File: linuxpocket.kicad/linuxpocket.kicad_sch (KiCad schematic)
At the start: 0 parts

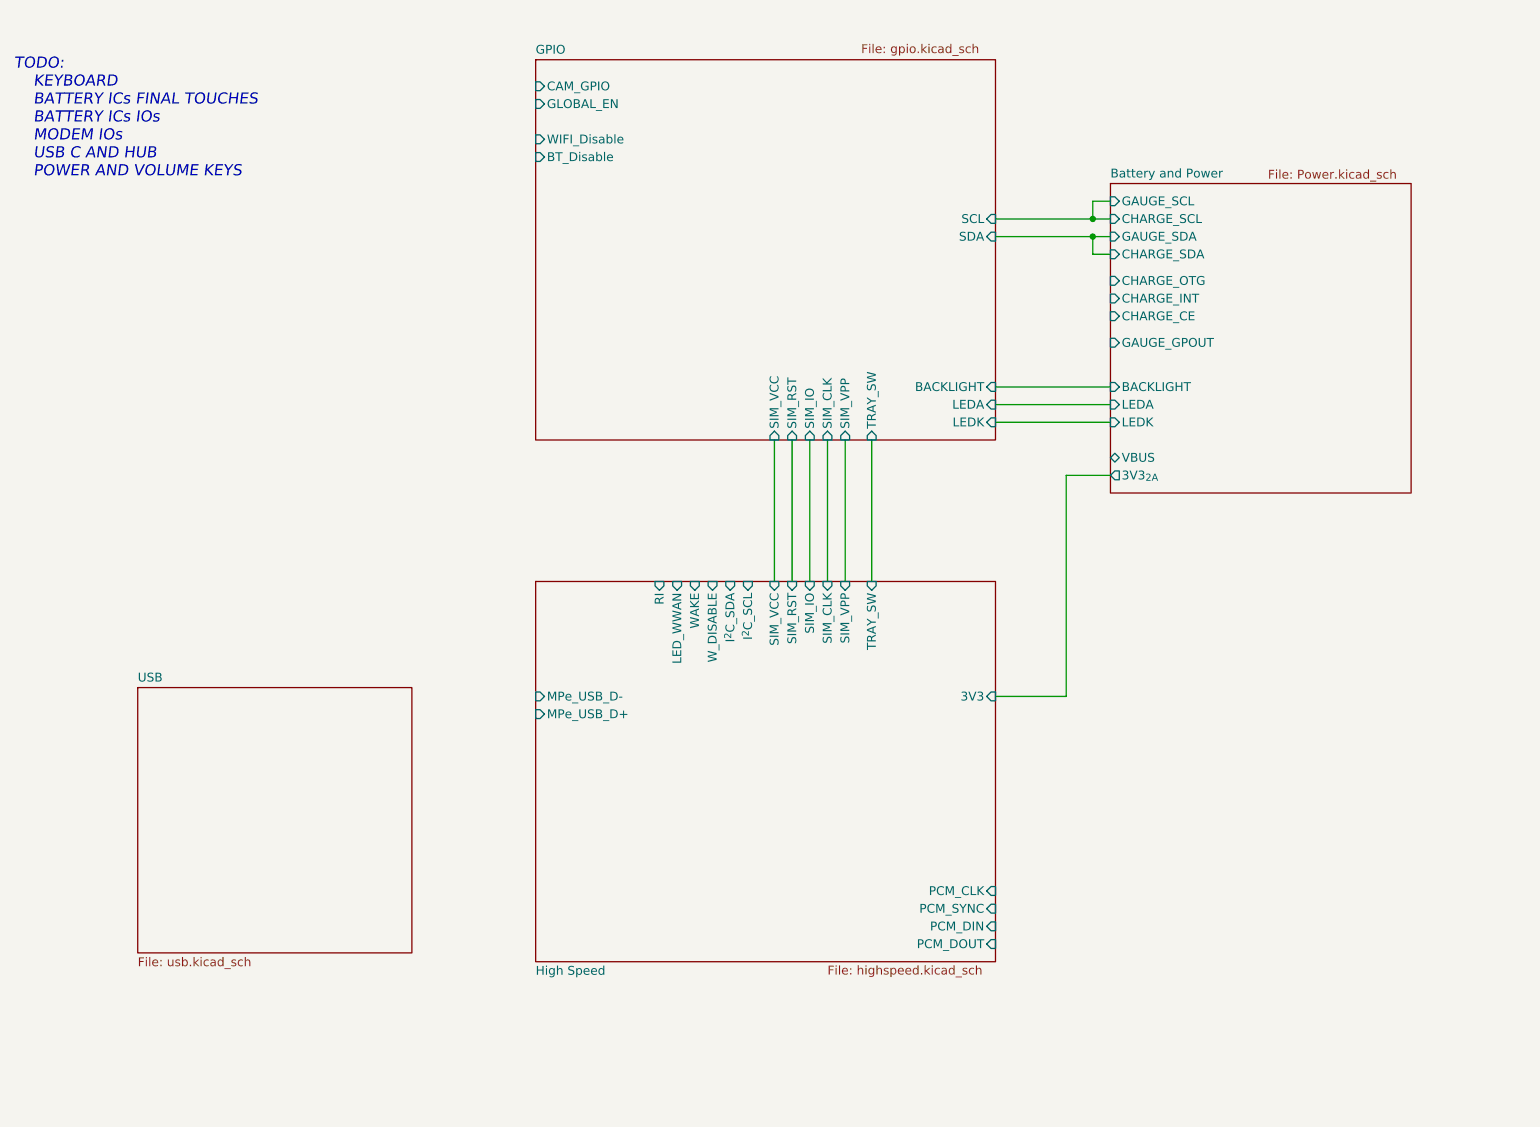
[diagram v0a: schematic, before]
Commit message: Add keyboard, improve many things etc.
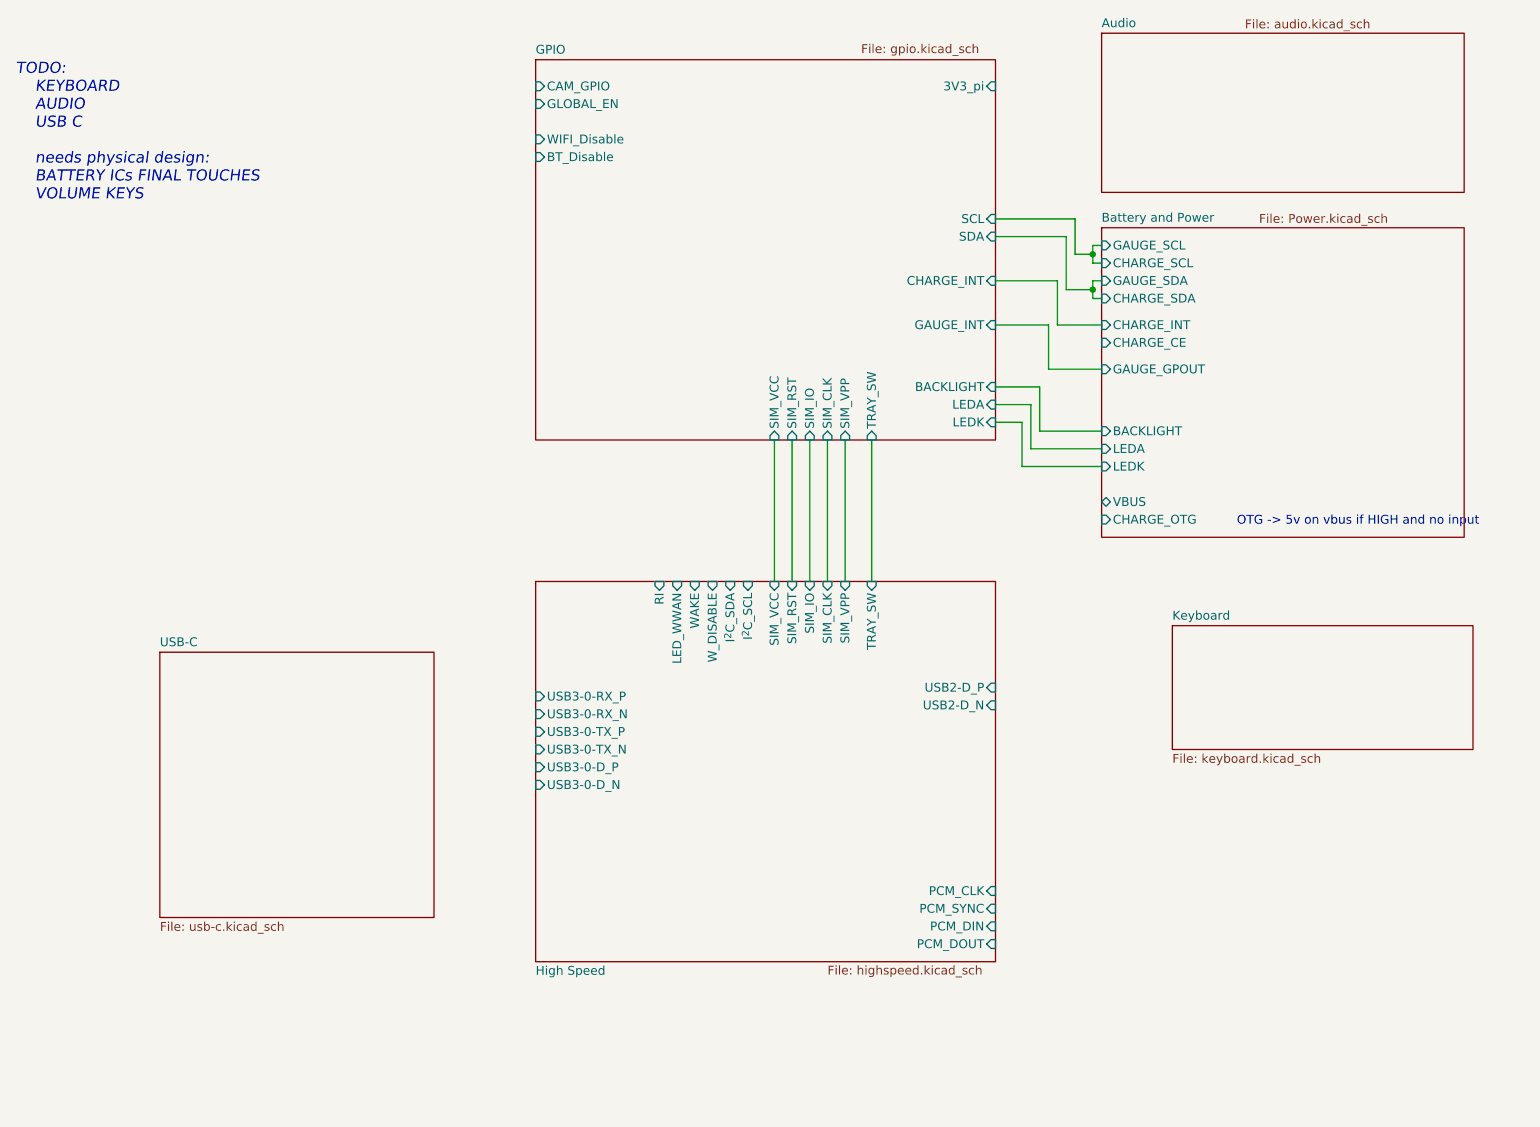
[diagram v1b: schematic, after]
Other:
- sheet USB renamed USB-C
- added sheet Audio (audio.kicad_sch)
- added sheet Keyboard (keyboard.kicad_sch)
- sheet Battery and Power ports: added none; removed 3V3_{2A}
- sheet GPIO ports: added 3V3_pi, CHARGE_INT, GAUGE_INT; removed none
- sheet High Speed ports: added USB2-D_N, USB2-D_P, USB3-0-D_N, USB3-0-D_P, USB3-0-RX_N, USB3-0-RX_P, USB3-0-TX_N, USB3-0-TX_P; removed 3V3, MPe_USB_D+, MPe_USB_D-
- sheet USB-C: file usb.kicad_sch -> usb-c.kicad_sch
- note added: "OTG -> 5v on vbus if HIGH and no input"
- note added: "TODO: KEYBOARD AUDIO USB C needs physical design: BATTERY ICs FINAL TOUCHES VOLUME KEYS"
- note removed: "TODO: KEYBOARD BATTERY ICs FINAL TOUCHES BATTERY ICs IOs MODEM IOs USB C AND HUB POWER AND VOLUME KEYS"

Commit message: Start with HDMI connector.
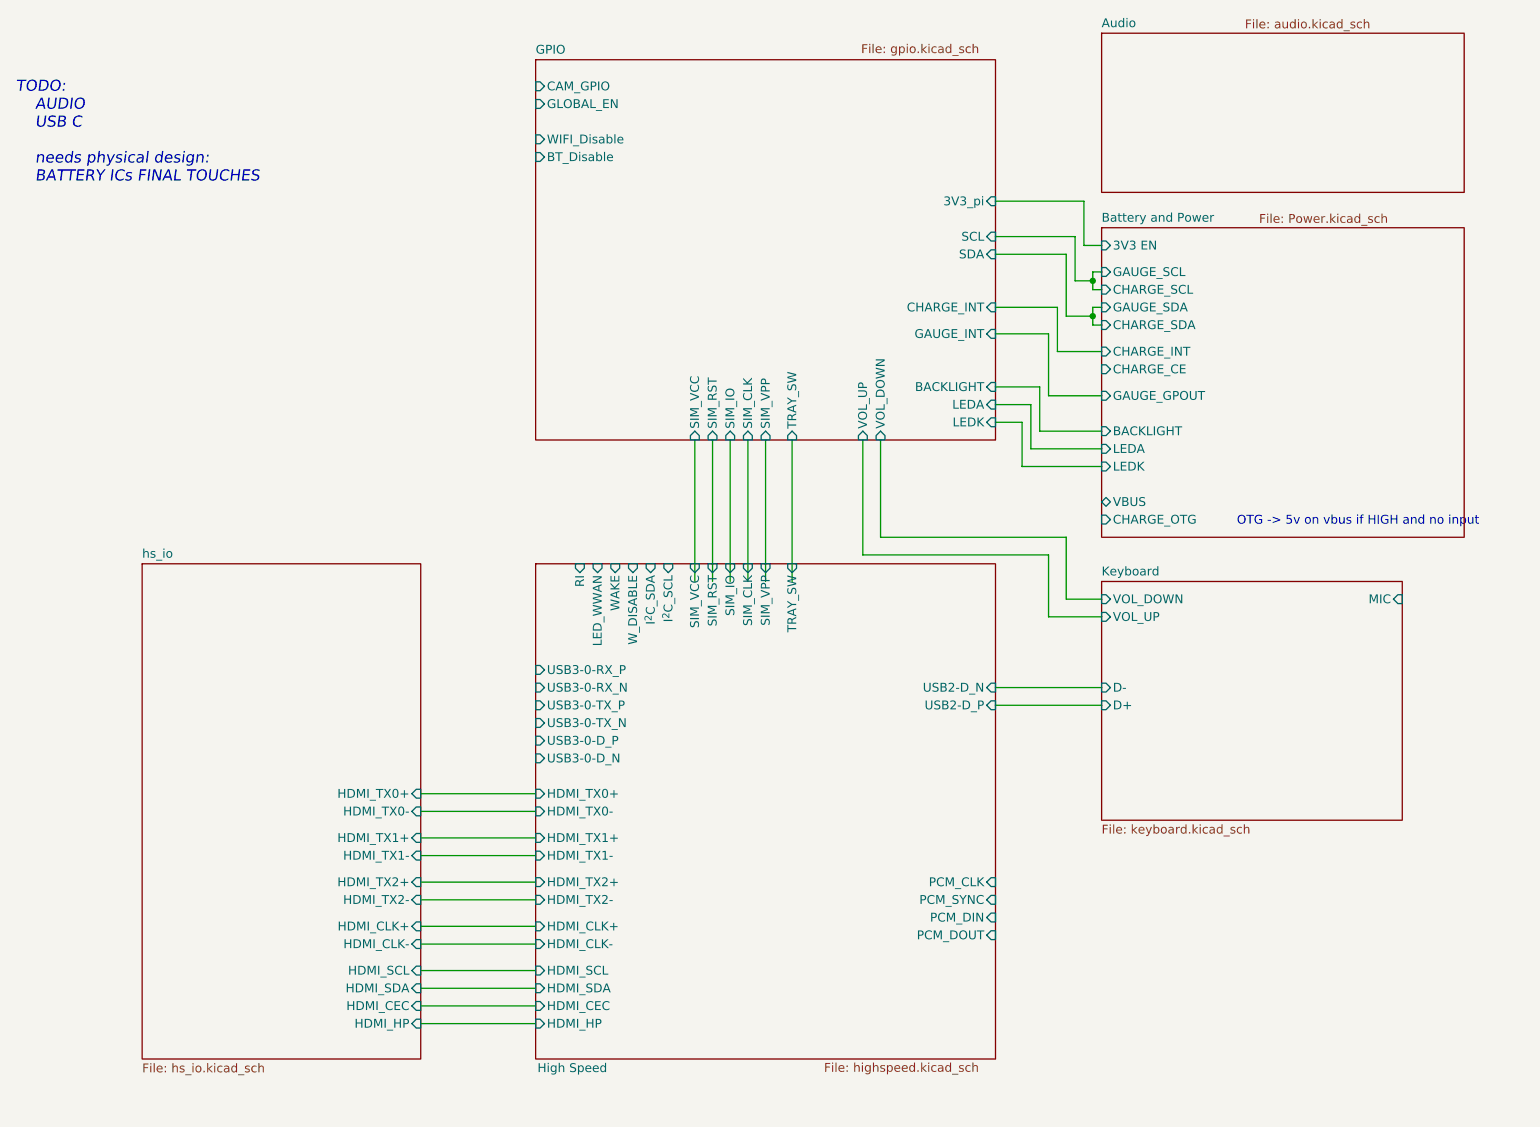
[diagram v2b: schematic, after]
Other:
- sheet USB-C renamed hs_io
- sheet Battery and Power ports: added 3V3 EN; removed none
- sheet GPIO ports: added VOL_DOWN, VOL_UP; removed none
- sheet High Speed ports: added HDMI_CEC, HDMI_CLK+, HDMI_CLK-, HDMI_HP, HDMI_SCL, HDMI_SDA, HDMI_TX0+, HDMI_TX0-, HDMI_TX1+, HDMI_TX1-, HDMI_TX2+, HDMI_TX2-; removed none
- sheet Keyboard ports: added D+, D-, MIC, VOL_DOWN, VOL_UP; removed none
- sheet hs_io: file usb-c.kicad_sch -> hs_io.kicad_sch
- sheet hs_io ports: added HDMI_CEC, HDMI_CLK+, HDMI_CLK-, HDMI_HP, HDMI_SCL, HDMI_SDA, HDMI_TX0+, HDMI_TX0-, HDMI_TX1+, HDMI_TX1-, HDMI_TX2+, HDMI_TX2-; removed none
- note added: "TODO: AUDIO USB C needs physical design: BATTERY ICs FINAL TOUCHES"
- note removed: "TODO: KEYBOARD AUDIO USB C needs physical design: BATTERY ICs FINAL TOUCHES VOLUME KEYS"

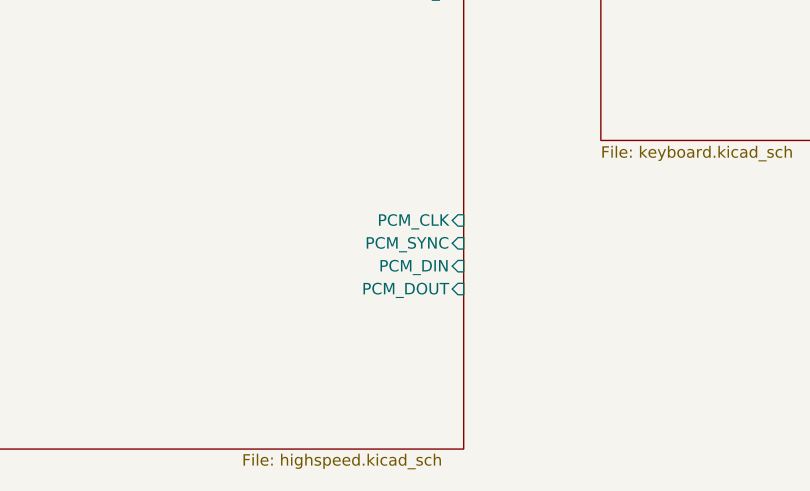
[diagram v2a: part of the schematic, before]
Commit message: Finish HDMI
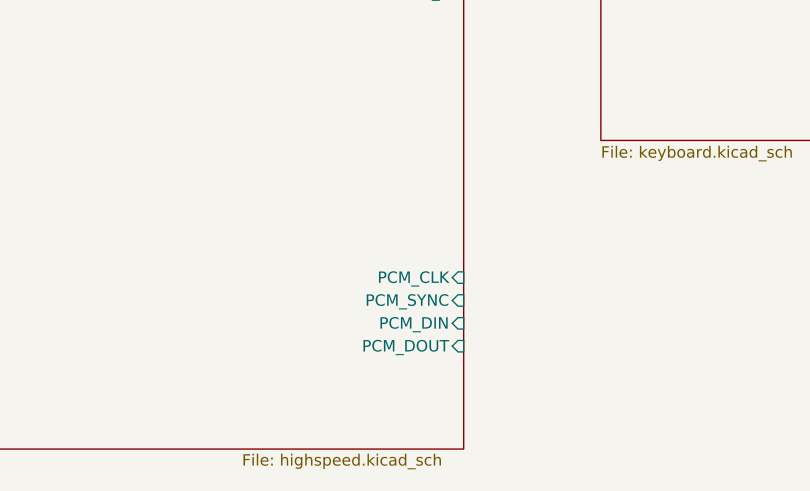
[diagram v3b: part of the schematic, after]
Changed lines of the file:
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@@
 	(title_block
 		(title "Overview")
-		(date "2024-19-10 - 2024-31-10")
+		(date "2024-10-19 - 2025-01-29")
 		(rev "Prototype v0")
 		(company "xamuel.xyz")
@@
 		)
 		(pin "PCM_DOUT" input
-			(at 172.72 154.94 0)
+			(at 172.72 161.29 0)
 			(effects
 				(font
@@
 		)
 		(pin "PCM_DIN" input
-			(at 172.72 152.4 0)
+			(at 172.72 158.75 0)
 			(effects
 				(font
@@
 		)
 		(pin "PCM_SYNC" input
-			(at 172.72 149.86 0)
+			(at 172.72 156.21 0)
 			(effects
 				(font
@@
 		)
 		(pin "PCM_CLK" input
-			(at 172.72 147.32 0)
-			(effects
-				(font
+			(at 172.72 153.67 0)
+			(effects
+				(font

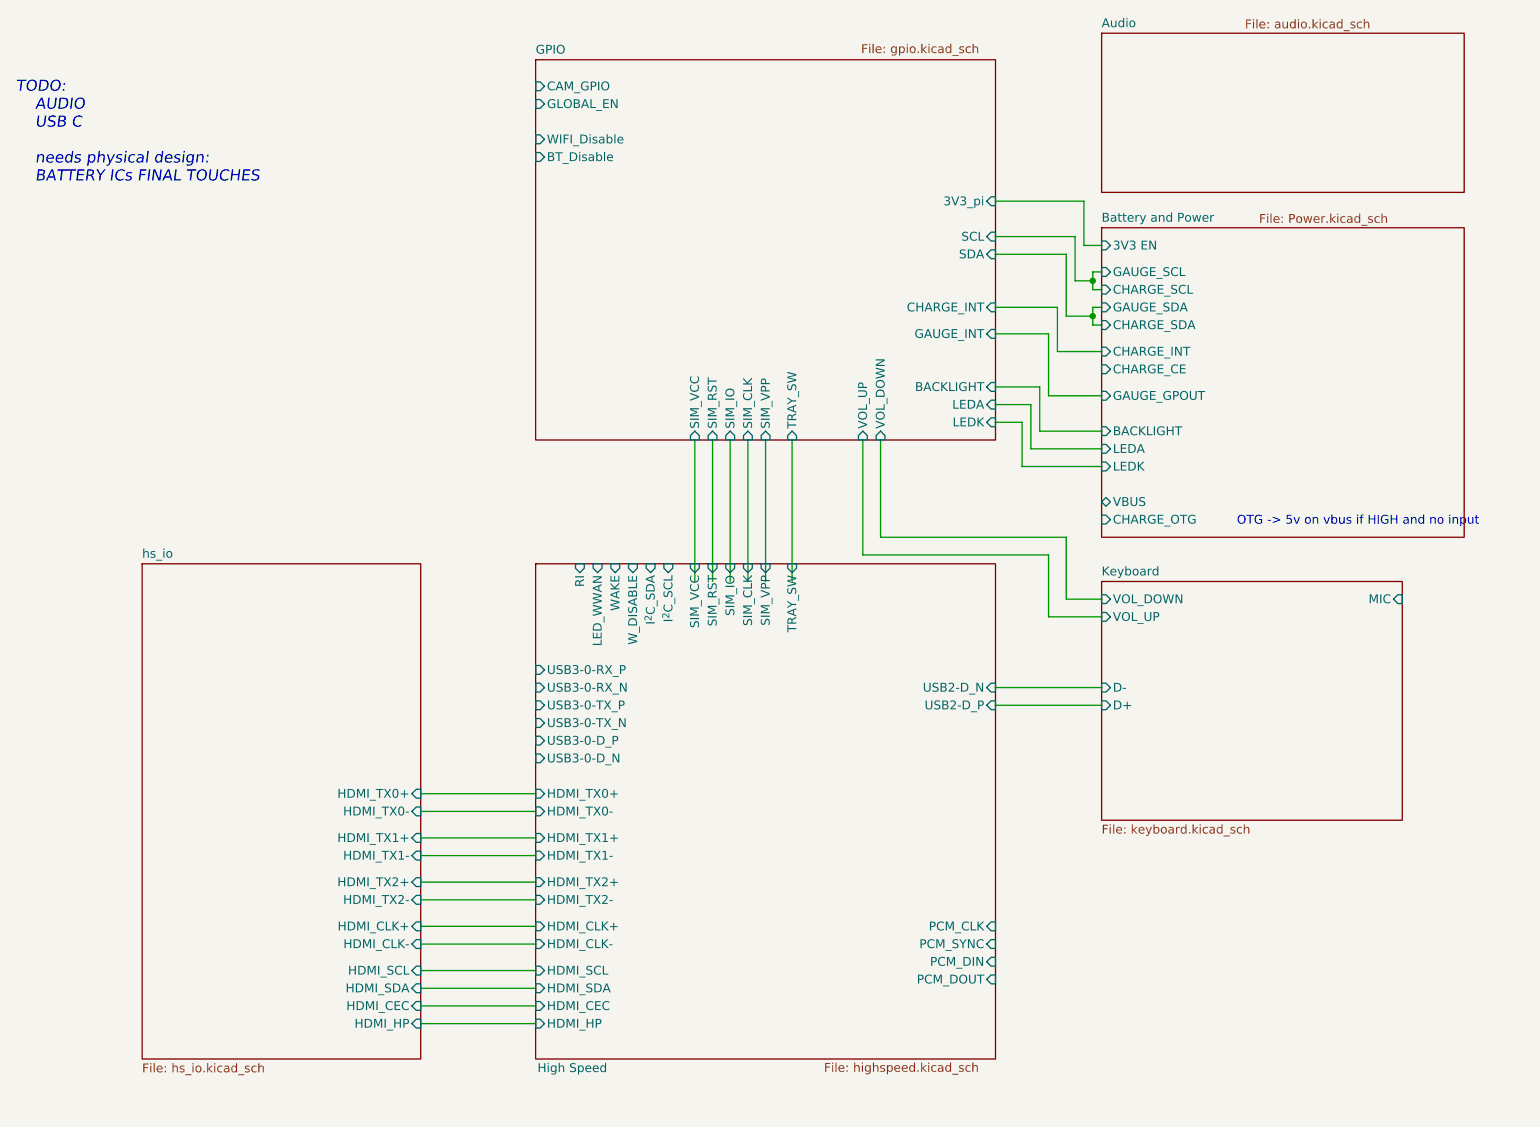
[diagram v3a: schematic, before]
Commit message: Finish USB-C. #1
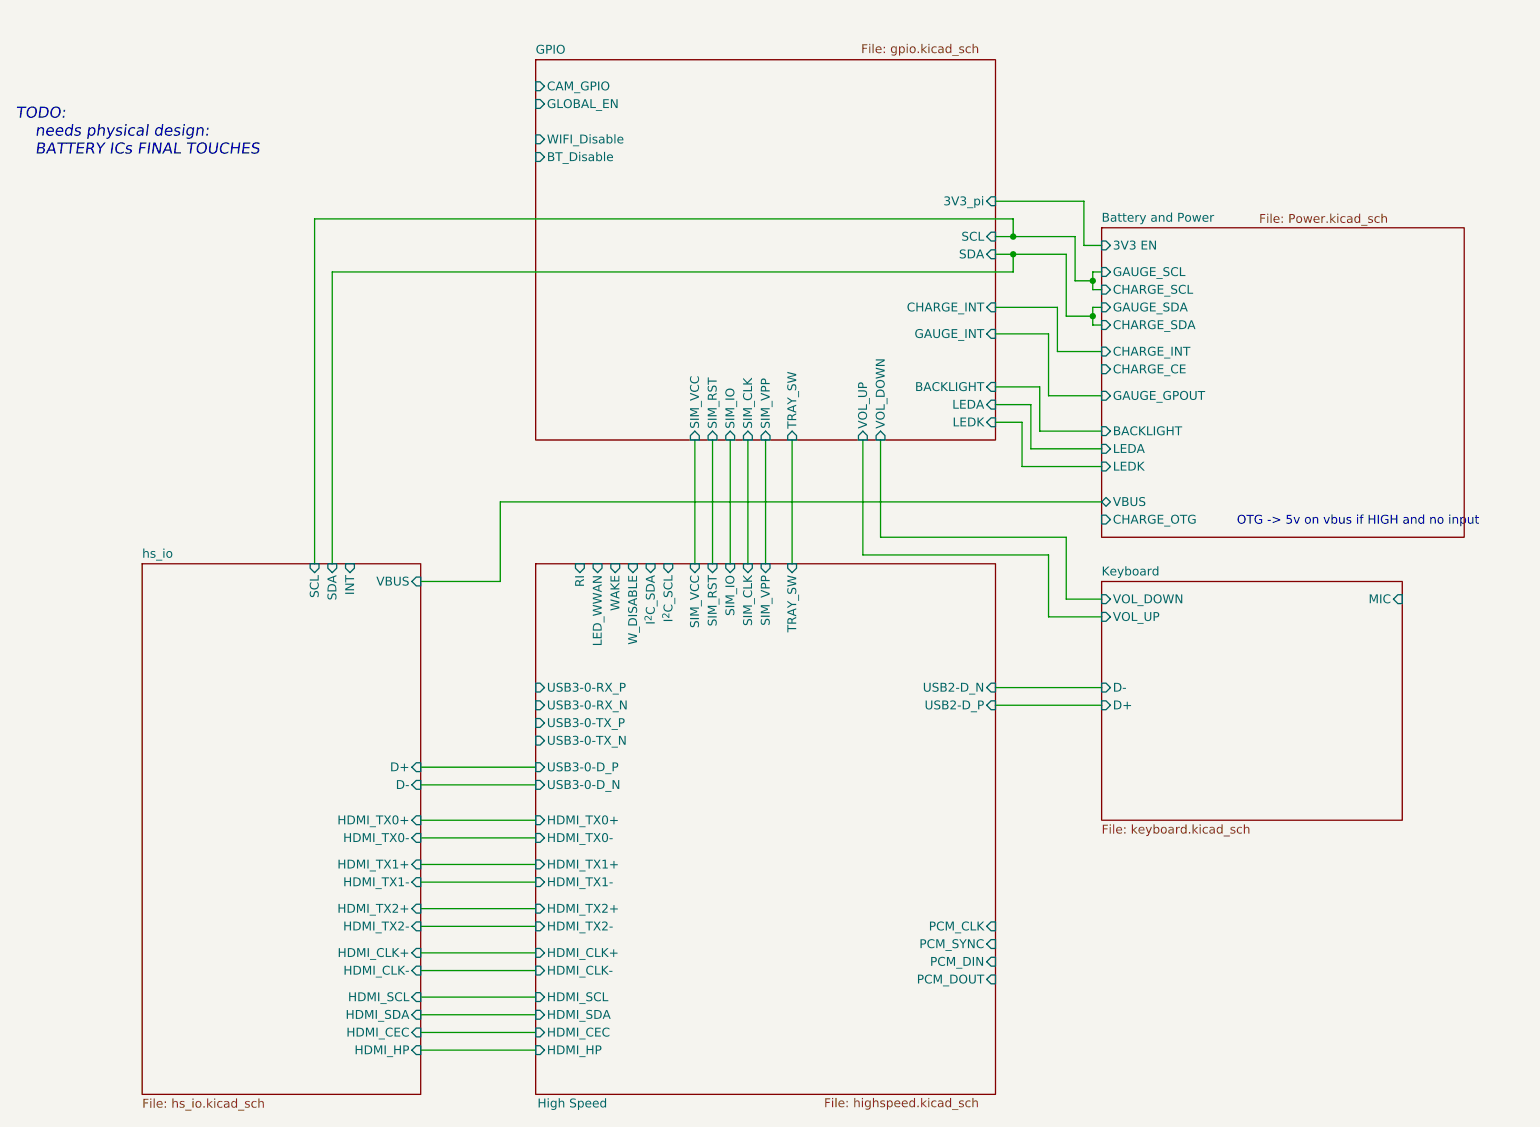
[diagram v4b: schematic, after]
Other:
- removed sheet Audio
- sheet hs_io ports: added D+, D-, INT, SCL, SDA, VBUS; removed none
- note added: "TODO: needs physical design: BATTERY ICs FINAL TOUCHES"
- note removed: "TODO: AUDIO USB C needs physical design: BATTERY ICs FINAL TOUCHES"
